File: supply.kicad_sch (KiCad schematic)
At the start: 72 parts, among them J301 Molex_Nano-Fit_1x2_SMD_105430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, Q301 DZDH0401DW, Q302 DZDH0401DW, Q303 DZDH0401DW, Q304 SQS401EN-T1_BE3, Q305 SQS401EN-T1_BE3, Q306 SQS401EN-T1_BE3, Q307 SQS401EN-T1_BE3, U301 AP62301WU-7, U302 AP62301WU-7, U303 AP62600SJ-7

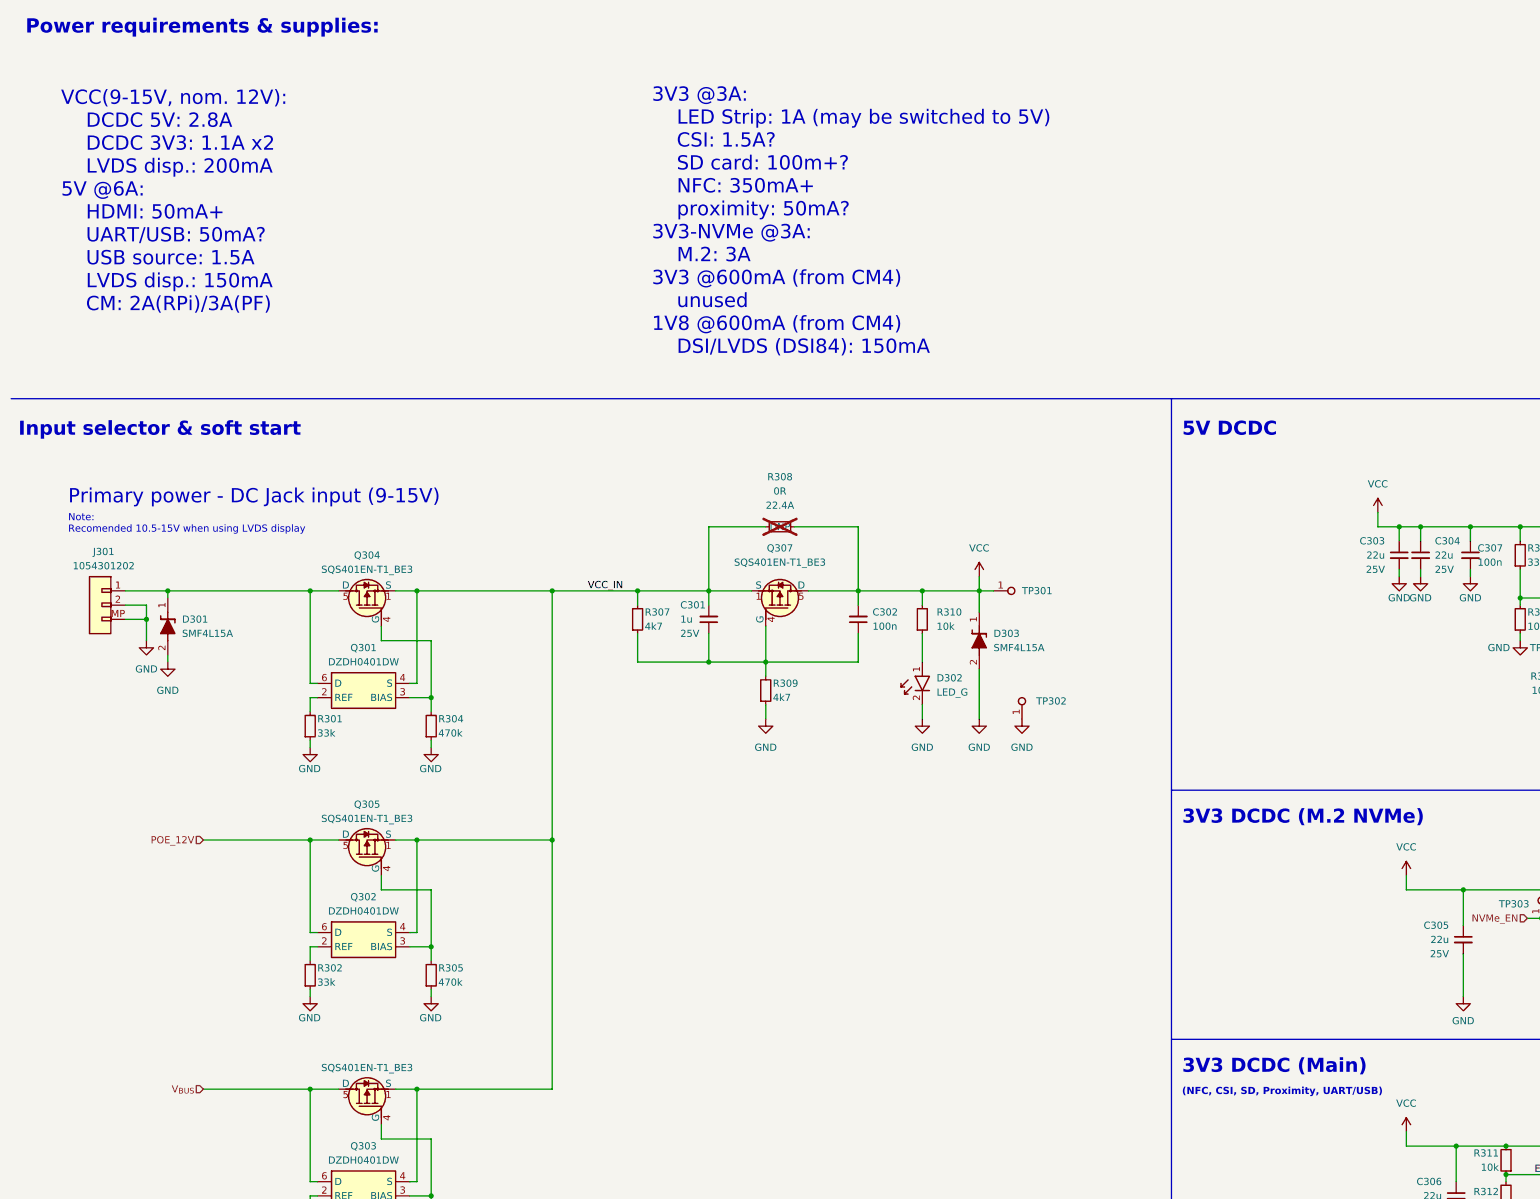
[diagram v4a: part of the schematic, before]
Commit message: [#56330] Clean ERC errors/warnings; update power supply notes
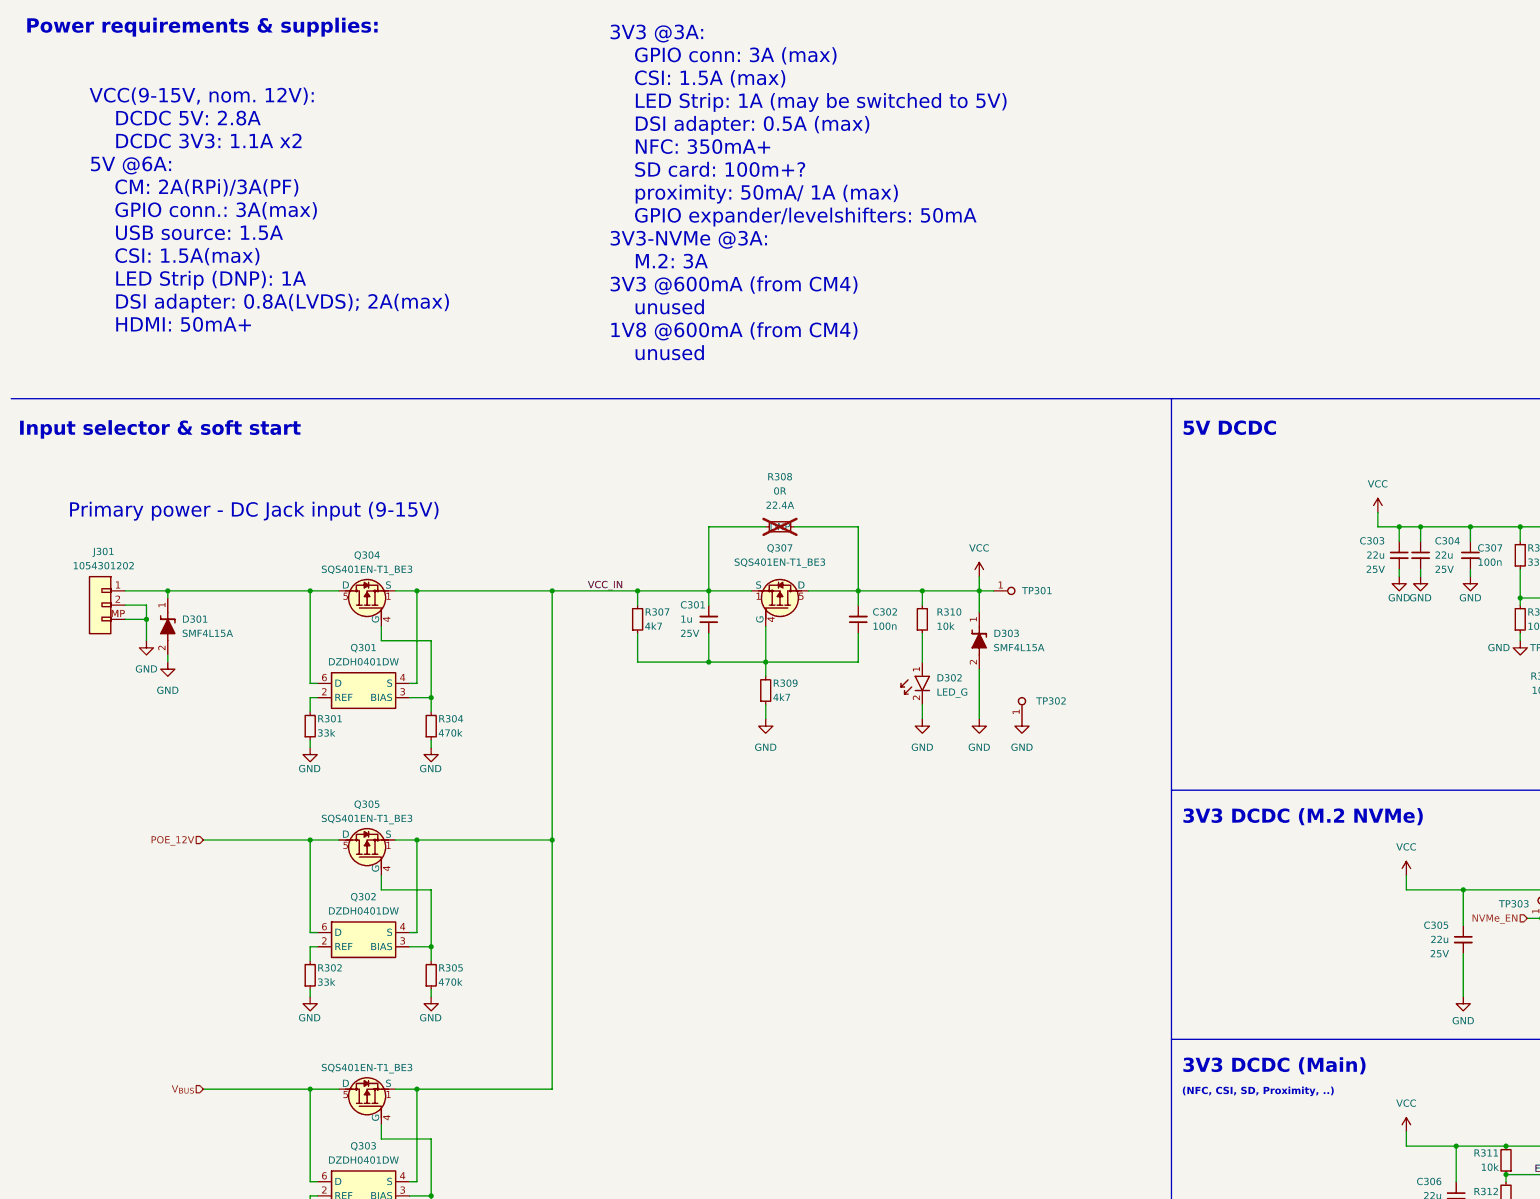
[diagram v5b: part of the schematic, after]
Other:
- note added: "(NFC, CSI, SD, Proximity, ..)"
- note added: "3V3 @3A: GPIO conn: 3A (max) CSI: 1.5A (max) LED Strip: 1A (may be switched to 5V) DSI adapter: 0.5A (max) NFC: 350mA+ SD card: 100m+? proximity: 50mA/ 1A (max) GPIO expander/levelshifters: 50mA 3V3-NVMe @3A: M.2: 3A 3V3 @600mA (from CM4) unused 1V8 @600mA (from CM4) unused"
- note added: "VCC(9-15V, nom. 12V): DCDC 5V: 2.8A DCDC 3V3: 1.1A x2 5V @6A: CM: 2A(RPi)/3A(PF) GPIO conn.: 3A(max) USB source: 1.5A CSI: 1.5A(max) LED Strip (DNP): 1A DSI adapter: 0.8A(LVDS); 2A(max) HDMI: 50mA+"
- note removed: "(NFC, CSI, SD, Proximity, UART/USB)"
- note removed: "3V3 @3A: LED Strip: 1A (may be switched to 5V) CSI: 1.5A? SD card: 100m+? NFC: 350mA+ proximity: 50mA? 3V3-NVMe @3A: M.2: 3A 3V3 @600mA (from CM4) unused 1V8 @600mA (from CM4) DSI/LVDS (DSI84): 150mA"
- note removed: "Note: Recomended 10.5-15V when using LVDS display"
- note removed: "VCC(9-15V, nom. 12V): DCDC 5V: 2.8A DCDC 3V3: 1.1A x2 LVDS disp.: 200mA 5V @6A: HDMI: 50mA+ UART/USB: 50mA? USB source: 1.5A LVDS disp.: 150mA CM: 2A(RPi)/3A(PF)"
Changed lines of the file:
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@@
     )
   )
-  (text "Note: \nRecomended 10.5-15V when using LVDS display"
-    (at 22.86 111.76 0)
-    (effects (font (size 1.27 1.27)) (justify left bottom))
-  )
-  (text " (NFC, CSI, SD, Proximity, UART/USB)" (at 220.98 212.09 0)
+  (text " (NFC, CSI, SD, Proximity, ..)" (at 220.98 212.09 0)
     (effects (font (size 1.27 1.27) (thickness 0.254) bold) (justify left bottom))
   )
@@
     (effects (font (size 1.27 1.27)) (justify left bottom))
   )
-  (text "Primary power - DC Jack input (9-15V)\n" (at 22.86 106.68 0)
+  (text "Primary power - DC Jack input (9-15V)\n" (at 22.86 109.22 0)
     (effects (font (size 2.54 2.54)) (justify left bottom))
   )
@@
     (effects (font (size 2.5 2.5) (thickness 0.5) bold) (justify left bottom))
   )
-  (text "3V3 @3A:\n	LED Strip: 1A (may be switched to 5V)\n	CSI: 1.5A?\n	SD card: 100m+?\n	NFC: 350mA+\n	proximity: 50mA?\n3V3-NVMe @3A:\n	M.2: 3A\n3V3 @600mA (from CM4)\n	unused\n1V8 @600mA (from CM4)\n	DSI/LVDS (DSI84): 150mA"
-    (at 127 80.01 0)
+  (text "3V3 @3A:\n	GPIO conn: 3A (max)\n	CSI: 1.5A (max)\n	LED Strip: 1A (may be switched to 5V)\n	DSI adapter: 0.5A (max)\n	NFC: 350mA+\n	SD card: 100m+?\n	proximity: 50mA/ 1A (max)\n	GPIO expander/levelshifters: 50mA\n3V3-NVMe @3A:\n	M.2: 3A\n3V3 @600mA (from CM4)\n	unused\n1V8 @600mA (from CM4)\n	unused"
+    (at 119.38 81.28 0)
     (effects (font (size 2.54 2.54)) (justify left bottom))
   )
-  (text "VCC(9-15V, nom. 12V):\n	DCDC 5V: 2.8A\n	DCDC 3V3: 1.1A x2\n	LVDS disp.: 200mA \n5V @6A:\n	HDMI: 50mA+\n	UART/USB: 50mA?\n	USB source: 1.5A\n	LVDS disp.: 150mA\n	CM: 2A(RPi)/3A(PF)\n"
-    (at 21.59 72.39 0)
+  (text "VCC(9-15V, nom. 12V):\n	DCDC 5V: 2.8A\n	DCDC 3V3: 1.1A x2\n5V @6A:\n	CM: 2A(RPi)/3A(PF)\n	GPIO conn.: 3A(max)\n	USB source: 1.5A\n	CSI: 1.5A(max)\n	LED Strip (DNP): 1A\n	DSI adapter: 0.8A(LVDS); 2A(max)\n	HDMI: 50mA+\n"
+    (at 26.67 76.2 0)
     (effects (font (size 2.54 2.54)) (justify left bottom))
   )
